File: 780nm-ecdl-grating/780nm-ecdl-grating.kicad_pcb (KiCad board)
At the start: 4 copper layers, 112.6 x 58.3 mm, 115 parts, among them IC1 OPA192IDR, IC2 OPA192IDR, IC3 OPA192IDR, IC4 OPA462IDDAR, IC5 OPA192IDR, J1 RP INPUT, J2 1755736, J3 TSW-103-07-G-S, J4 1755736, J5 MON OUT, J7 1715747, U1 ADR4550, U2 BAV199Q-7-F

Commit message: alas completed the grating controller!
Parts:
- moved C25 2.81 mm to (233.3, 45.0)
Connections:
- J1 pad 3: (no net) -> GND
- J1 pad 4: (no net) -> GND
- J1 pad 5: (no net) -> GND
- SUM OUT pad 1: SUM_OUT -> CMD_IN
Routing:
- net SUM_OUT: track 36.3 -> 23.2 mm
- net CMD_IN: track 25.1 -> 36.6 mm
- net +155V: track 33.6 -> 45.0 mm
- net GND: track 6.19 -> 12.7 mm, vias 8 -> 122

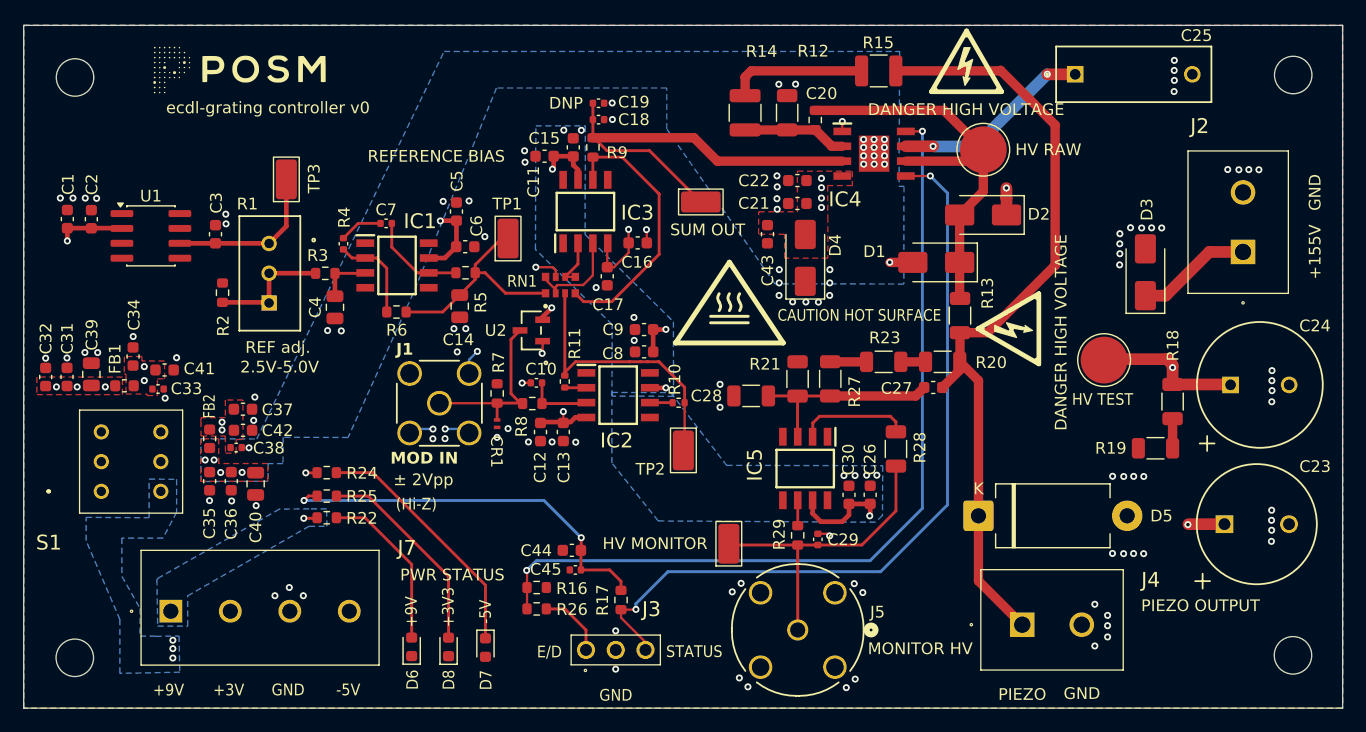
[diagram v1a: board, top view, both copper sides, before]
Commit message: fixed vias
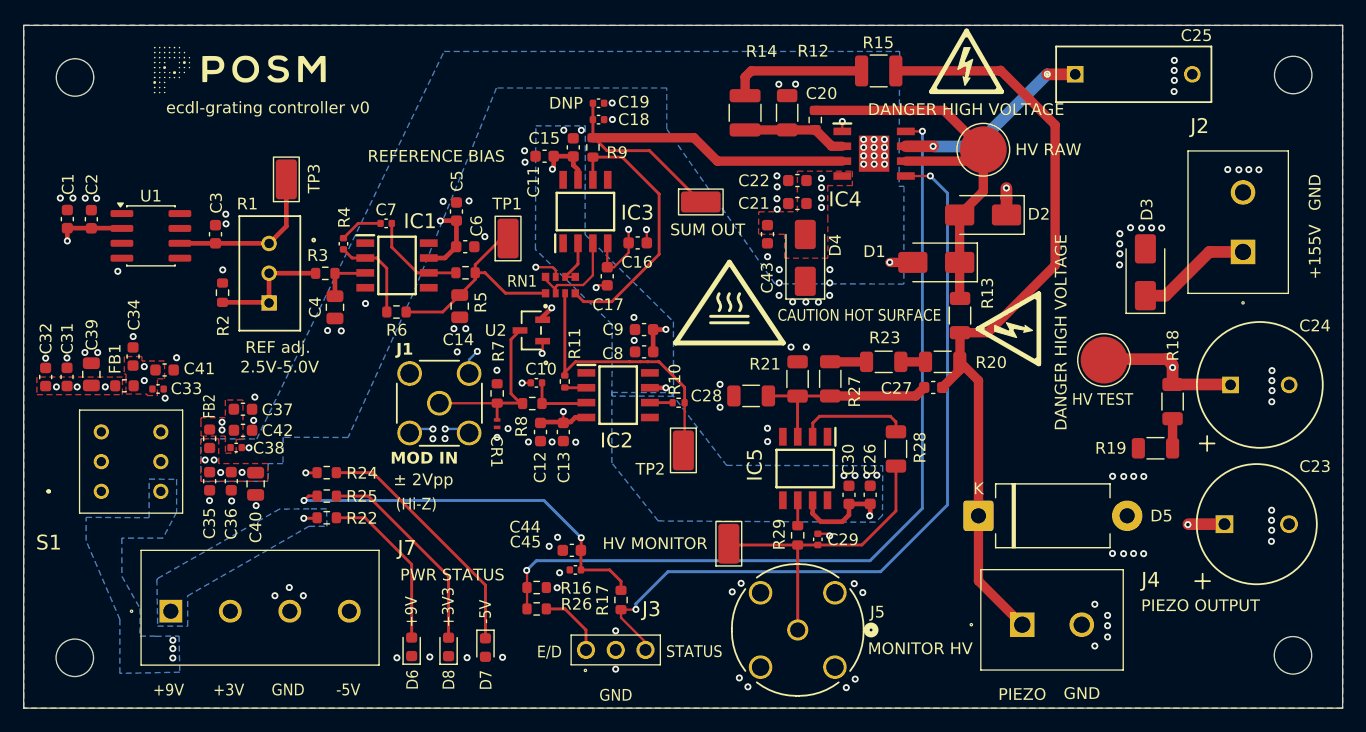
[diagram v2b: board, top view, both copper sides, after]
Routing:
- net GND: track 12.7 -> 13.7 mm, vias 122 -> 139
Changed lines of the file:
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@@
 		(tags "resistor")
 		(property "Reference" "R26"
-			(at 3.018148 0.05 0)
+			(at 3.395 -0.395 0)
 			(layer "F.SilkS")
 			(effects
@@
 		(tags "capacitor")
 		(property "Reference" "C43"
-			(at -3.095 0.02 90)
+			(at -3.715 -0.02 90)
 			(layer "F.SilkS")
 			(effects
@@
 		(tags "capacitor")
 		(property "Reference" "C44"
-			(at 3.04079 -0.025 0)
+			(at 3.995 1.985 0)
 			(layer "F.SilkS")
 			(effects
@@
 		(tags "resistor")
 		(property "Reference" "R7"
-			(at 2.653069 0.125 90)
+			(at 3.598069 0.11 90)
 			(layer "F.SilkS")
 			(effects
@@
 		(tags "capacitor")
 		(property "Reference" "C45"
-			(at 2.525 0.05 0)
+			(at 4.26 2.39 0)
 			(layer "F.SilkS")
 			(effects
@@
 		(tags "resistor")
 		(property "Reference" "R16"
-			(at 3.005 0.09 0)
+			(at 3.365 0.06 0)
 			(layer "F.SilkS")
 			(effects
@@
 	)
 	(segment
+		(start 192.54 63.05)
+		(end 192.35 63.24)
+		(width 0.2)
+		(layer "F.Cu")
+		(net "GND")
+	)
+	(segment
 		(start 186.045 71.375)
 		(end 186.03 71.39)
@@
 		(net "GND")
 	)
+	(segment
+		(start 193.3 63.05)
+		(end 192.54 63.05)
+		(width 0.2)
+		(layer "F.Cu")
+		(net "GND")
+	)
+	(via
+		(at 208.99 68.32)
+		(size 0.6)
+		(drill 0.3)
+		(layers "F.Cu" "B.Cu")
+		(free yes)
+		(net "GND")
+	)
 	(via
 		(at 160.75 57.8)
@@
 	)
 	(via
+		(at 210.3 68.32)
+		(size 0.6)
+		(drill 0.3)
+		(layers "F.Cu" "B.Cu")
+		(free yes)
+		(net "GND")
+	)
+	(via
 		(at 159.34 81.43)
 		(size 0.6)
@@
 	)
 	(via
+		(at 183.88 70.3)
+		(size 0.6)
+		(drill 0.3)
+		(layers "F.Cu" "B.Cu")
+		(free yes)
+		(net "GND")
+	)
+	(via
 		(at 202.93 73.46)
 		(size 0.6)
@@
 	)
 	(via
+		(at 206.99 60.6)
+		(size 0.6)
+		(drill 0.3)
+		(layers "F.Cu" "B.Cu")
+		(free yes)
+		(net "GND")
+	)
+	(via
 		(at 237.4 79.37)
 		(size 0.6)
@@
 	)
 	(via
+		(at 206.98 75.25)
+		(size 0.6)
+		(drill 0.3)
+		(layers "F.Cu" "B.Cu")
+		(free yes)
+		(net "GND")
+	)
+	(via
 		(at 192.35 63.24)
 		(size 0.6)
@@
 	)
 	(via
+		(at 172.66 64.6)
+		(size 0.6)
+		(drill 0.3)
+		(layers "F.Cu" "B.Cu")
+		(free yes)
+		(net "GND")
+	)
+	(via
 		(at 186.28 52.53)
 		(size 0.6)
@@
 	)
 	(via
+		(at 188.34 85.33)
+		(size 0.6)
+		(drill 0.3)
+		(layers "F.Cu" "B.Cu")
+		(free yes)
+		(net "GND")
+	)
+	(via
 		(at 207.98 62.84)
 		(size 0.6)
@@
 	)
 	(via
+		(at 189.23 87.59)
+		(size 0.6)
+		(drill 0.3)
+		(layers "F.Cu" "B.Cu")
+		(free yes)
+		(net "GND")
+	)
+	(via
 		(at 209.13 64.46)
 		(size 0.6)
@@
 	)
 	(via
+		(at 175.34 94.85)
+		(size 0.6)
+		(drill 0.3)
+		(layers "F.Cu" "B.Cu")
+		(free yes)
+		(net "GND")
+	)
+	(via
 		(at 247.23 53.18)
 		(size 0.6)
@@
 	)
 	(via
+		(at 151.51 61.85)
+		(size 0.6)
+		(drill 0.3)
+		(layers "F.Cu" "B.Cu")
+		(free yes)
+		(net "GND")
+	)
+	(via
 		(at 237.98 58.13)
 		(size 0.6)
@@
 	)
 	(via
+		(at 184.36 94.81)
+		(size 0.6)
+		(drill 0.3)
+		(layers "F.Cu" "B.Cu")
+		(free yes)
+		(net "GND")
+	)
+	(via
+		(at 189.02 88.87)
+		(size 0.6)
+		(drill 0.3)
+		(layers "F.Cu" "B.Cu")
+		(free yes)
+		(net "GND")
+	)
+	(via
 		(at 210.26 64.47)
 		(size 0.6)
@@
 	)
 	(via
+		(at 206.99 76.39)
+		(size 0.6)
+		(drill 0.3)
+		(layers "F.Cu" "B.Cu")
+		(free yes)
+		(net "GND")
+	)
+	(via
 		(at 162.71 76.92)
 		(size 0.6)
@@
 	)
 	(via
+		(at 178.15 94.78)
+		(size 0.6)
+		(drill 0.3)
+		(layers "F.Cu" "B.Cu")
+		(free yes)
+		(net "GND")
+	)
+	(via
 		(at 236.44 85.94)
 		(size 0.6)
@@
 	)
 	(via
+		(at 181.33 94.84)
+		(size 0.6)
+		(drill 0.3)
+		(layers "F.Cu" "B.Cu")
+		(free yes)
+		(net "GND")
+	)
+	(via
 		(at 152.82 67.42)
 		(size 0.6)
@@
 	)
 	(via
+		(at 160.47 61.73)
+		(size 0.6)
+		(drill 0.3)
+		(layers "F.Cu" "B.Cu")
+		(free yes)
+		(net "GND")
+	)
+	(via
 		(at 213.71 97.4)
 		(size 0.6)
@@
 		(size 0.6)
 		(drill 0.3)
+		(layers "F.Cu" "B.Cu")
+		(free yes)
+		(net "GND")
+	)
+	(via
+		(at 189.06 84.56)
+		(size 0.6)
+		(drill 0.3)
